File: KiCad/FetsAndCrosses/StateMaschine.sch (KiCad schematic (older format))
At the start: 0 parts

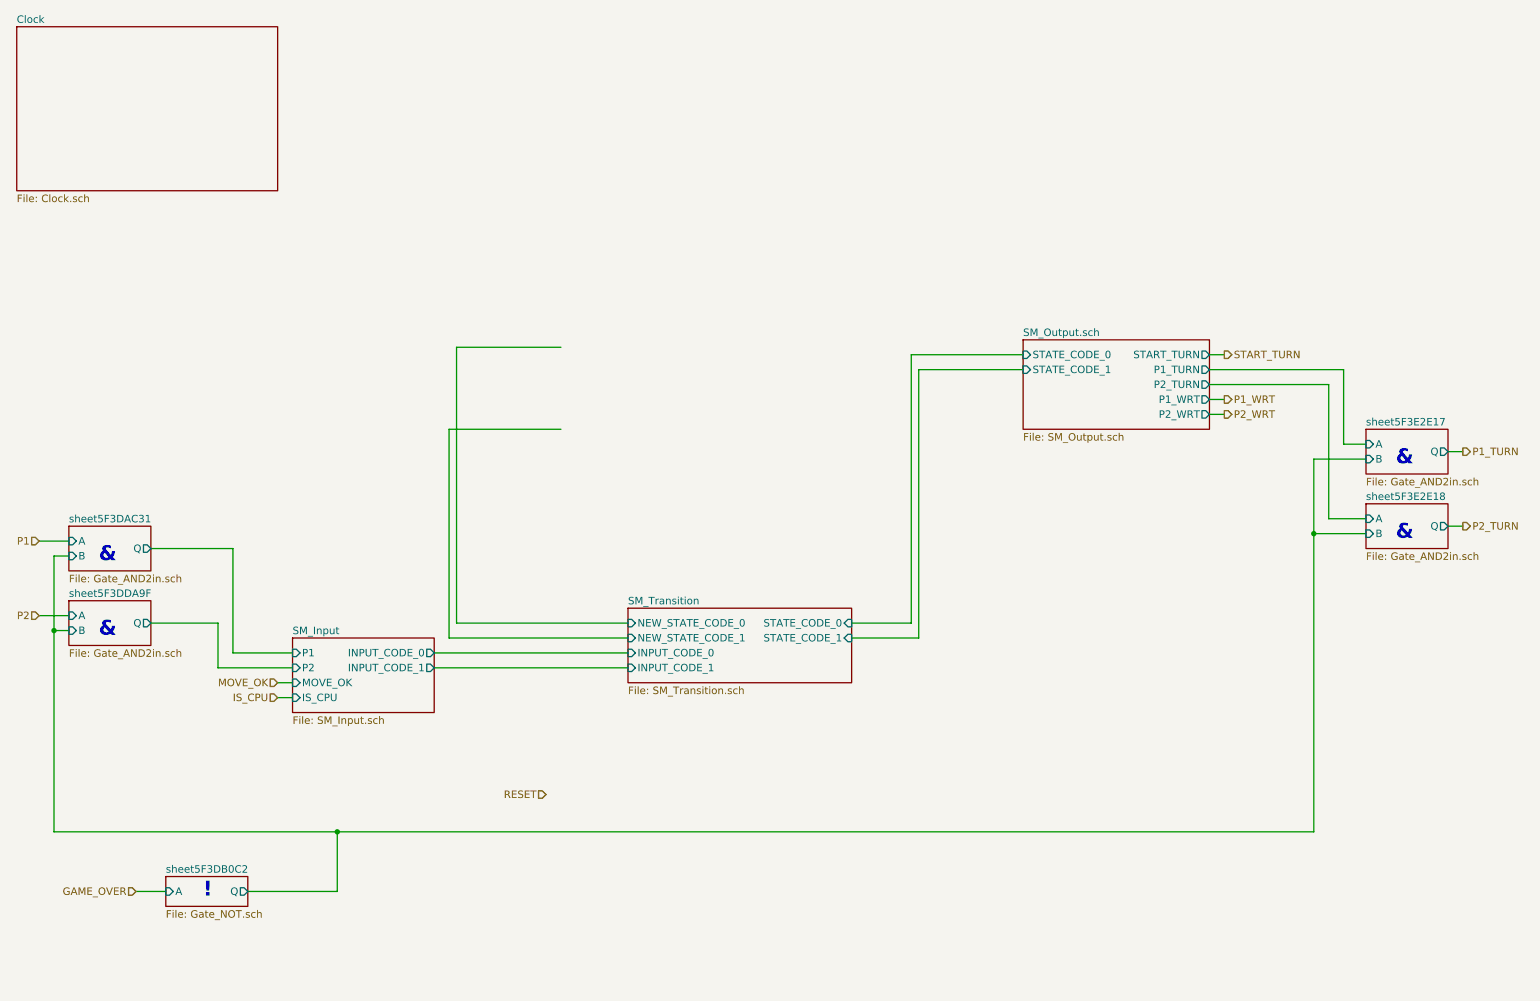
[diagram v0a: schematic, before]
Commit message: Reworked everything to use Buses
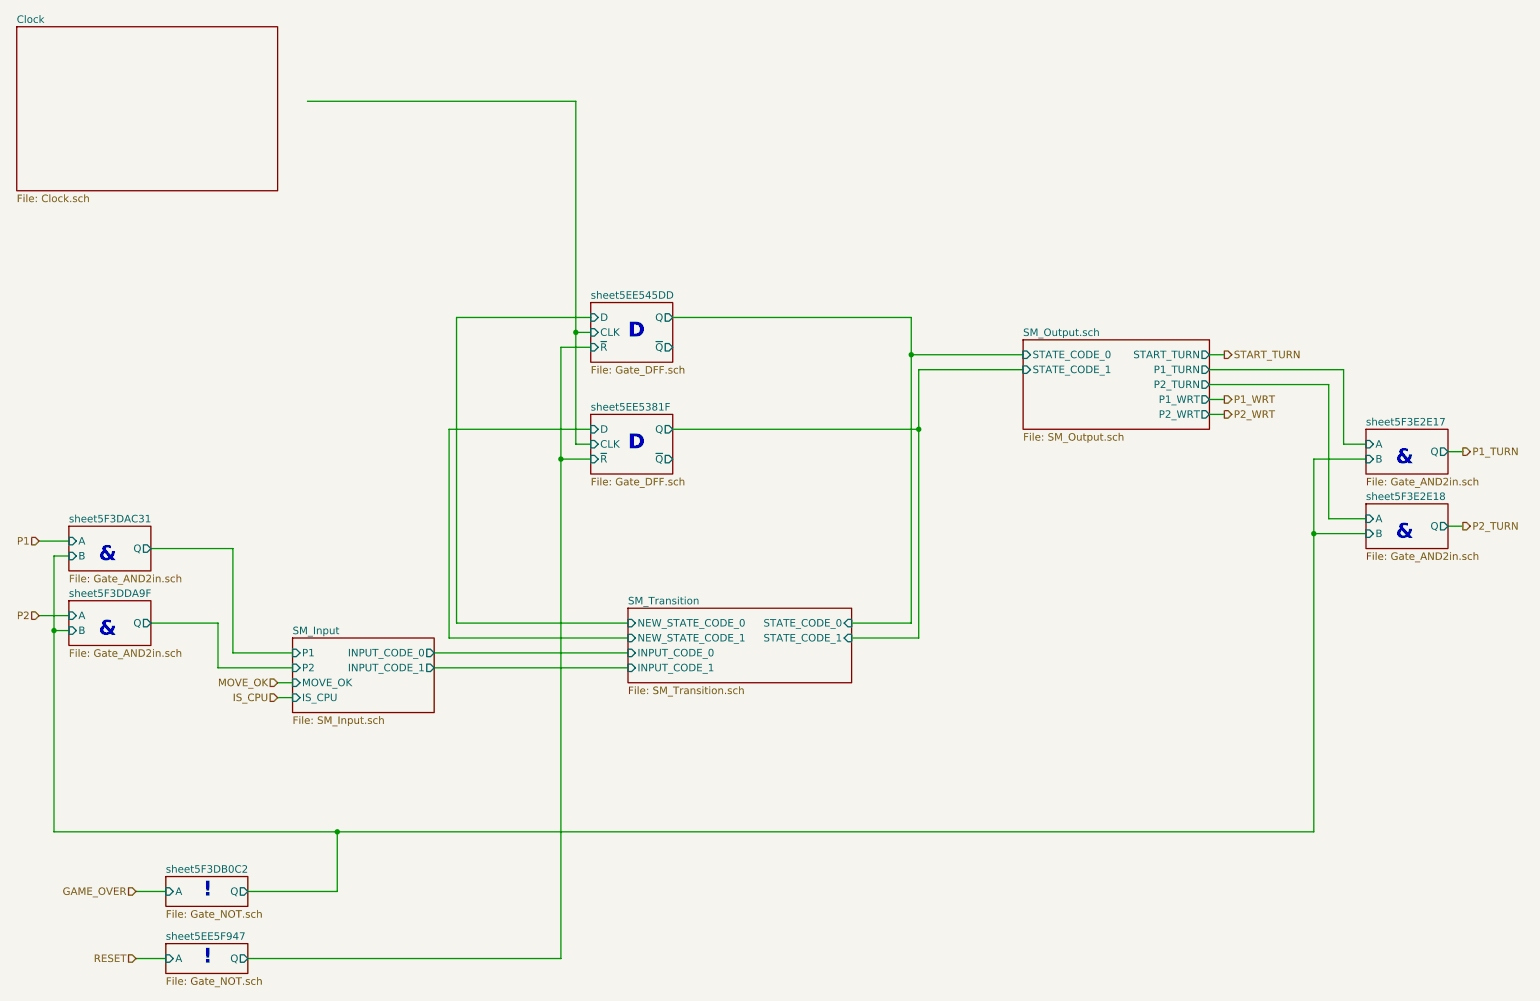
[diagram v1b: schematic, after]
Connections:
- wire segments 48 -> 63
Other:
- note added: "D"
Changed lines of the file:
@@
 $Descr A4 11693 8268
 encoding utf-8
-Sheet 167 215
+Sheet 170 400
 Title ""
 Date ""
@@
 	7700 3000 7000 3000
 Wire Wire Line
-	7000 3000 7000 4800
+	7000 3000 7000 3400
 Wire Wire Line
 	7000 4800 6550 4800
@@
 	3850 4800 3850 3400
 Wire Wire Line
-	3850 3400 4600 3400
-Wire Wire Line
 	5050 4700 3900 4700
 Wire Wire Line
-	3900 4700 3900 2850
-Wire Wire Line
-	3900 2850 4600 2850
-Text HLabel 4500 5850 0    50   Input ~ 0
+	3900 4700 3900 2650
+Text HLabel 1750 6950 0    50   Input ~ 0
 RESET
 Text HLabel 9050 2900 2    50   Output ~ 0
@@
 Connection ~ 9650 4100
 Connection ~ 3100 6100
+$Sheet
+S 4800 3300 550  400
+U 5EE53826
+F0 "sheet5EE5381F" 50
+F1 "Gate_DFF.sch" 50
+F2 "D" I L 4800 3400 50
+F3 "CLK" I L 4800 3500 50
+F4 "Q" O R 5350 3400 50
+F5 "~Q" O R 5350 3600 50
+F6 "~R" I L 4800 3600 50
+$EndSheet
+Text Notes 5050 3550 0    100  ~ 20
+D
+$Sheet
+S 4800 2550 550  400
+U 5EE545E4
+F0 "sheet5EE545DD" 50
+F1 "Gate_DFF.sch" 50
+F2 "D" I L 4800 2650 50
+F3 "CLK" I L 4800 2750 50
+F4 "Q" O R 5350 2650 50
+F5 "~Q" O R 5350 2850 50
+F6 "~R" I L 4800 2850 50
+$EndSheet
+Text Notes 5050 2800 0    100  ~ 20
+D
+Wire Wire Line
+	3900 2650 4800 2650
+Wire Wire Line
+	3850 3400 4800 3400
+Wire Wire Line
+	4800 3500 4700 3500
+Wire Wire Line
+	4700 3500 4700 2750
+Wire Wire Line
+	4700 2750 4800 2750
+Wire Wire Line
+	4700 2750 4700 1200
+Wire Wire Line
+	4700 1200 2900 1200
+Connection ~ 4700 2750
+Wire Wire Line
+	4800 3600 4600 3600
+Wire Wire Line
+	4600 3600 4600 2850
+Wire Wire Line
+	4600 2850 4800 2850
+Wire Wire Line
+	4600 3600 4600 6950
+Connection ~ 4600 3600
+$Sheet
+S 1950 6850 550  200
+U 5EE5F94B
+F0 "sheet5EE5F947" 50
+F1 "Gate_NOT.sch" 50
+F2 "A" I L 1950 6950 50
+F3 "Q" O R 2500 6950 50
+$EndSheet
+Text Notes 2200 7000 0    100  ~ 20
+!
+Wire Wire Line
+	2500 6950 4600 6950
+Wire Wire Line
+	1750 6950 1950 6950
+Wire Wire Line
+	6950 2900 6950 2650
+Wire Wire Line
+	6950 2650 5350 2650
+Connection ~ 6950 2900
+Wire Wire Line
+	5350 3400 7000 3400
+Connection ~ 7000 3400
+Wire Wire Line
+	7000 3400 7000 4800
 $EndSCHEMATC

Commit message: Schematic Done, Footprints assigned, ERC OK.
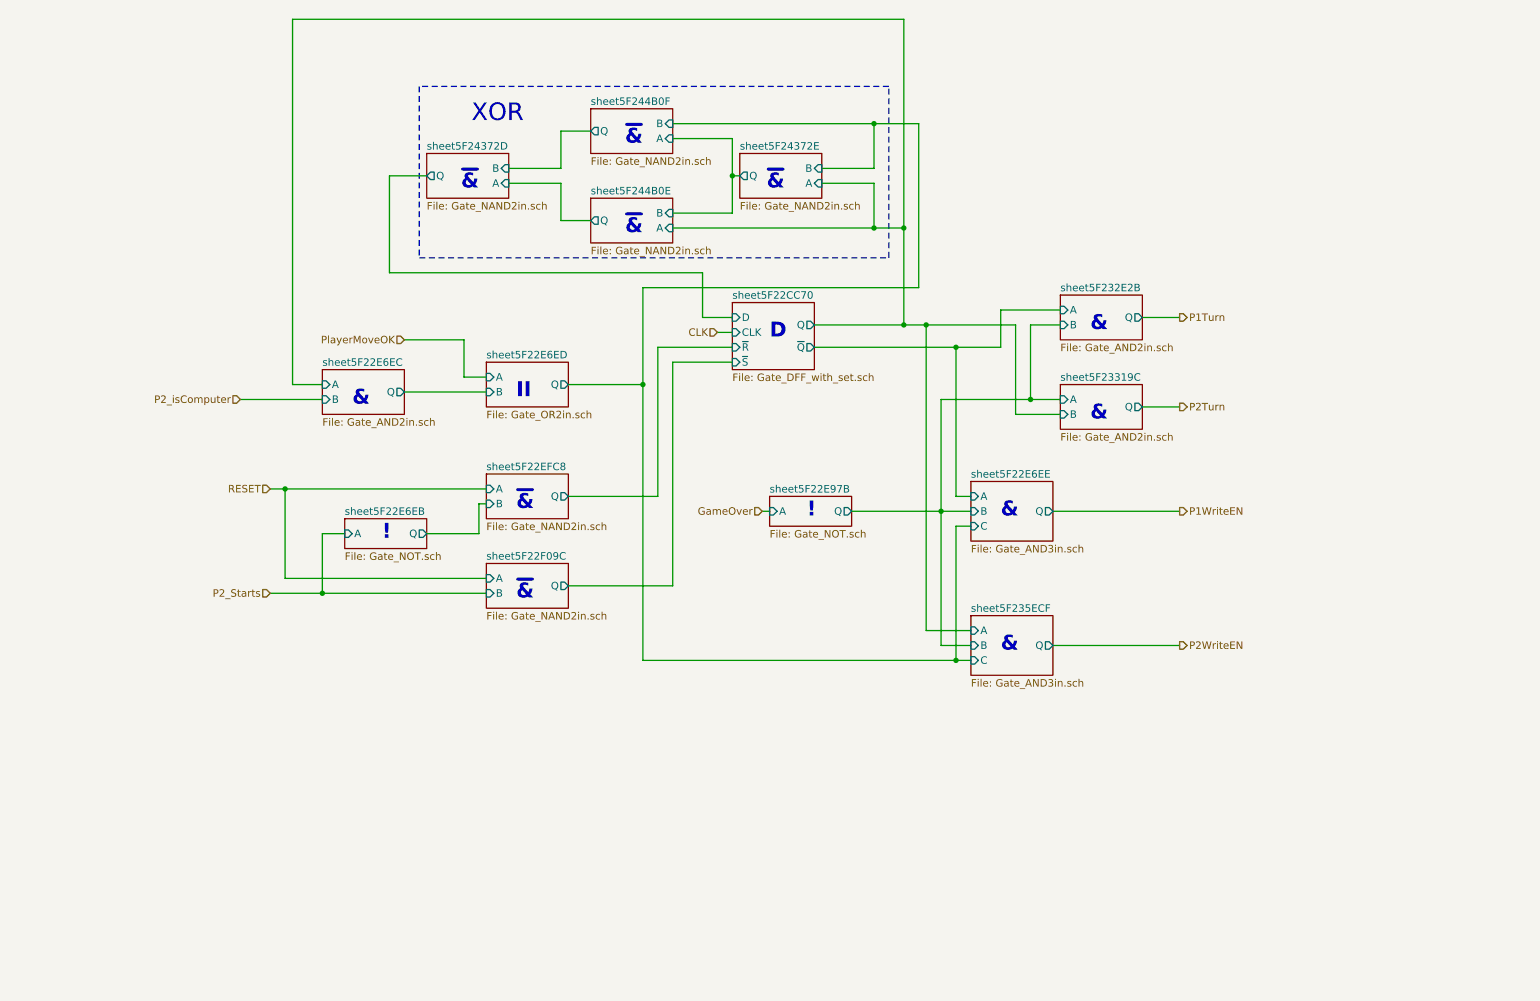
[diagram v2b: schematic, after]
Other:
- note added: "II"
- note added: "XOR"
- note added: "~&"

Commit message: First Draft Schematic Updates
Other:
- note added: "Accept Move Logic\n"
- note added: "Output Decoding"
- note added: "Select Right Player on Reset"
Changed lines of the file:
@@
 $Descr A4 11693 8268
 encoding utf-8
-Sheet 159 389
+Sheet 149 360
 Title ""
 Date "2020-07-05"
@@
 $EndSheet
 $Sheet
-S 3150 4000 550  200
+S 3100 5400 550  200
 U 5F22E6F2
 F0 "sheet5F22E6EB" 50
 F1 "Gate_NOT.sch" 50
-F2 "A" I L 3150 4100 50
-F3 "Q" O R 3700 4100 50
+F2 "A" I L 3100 5500 50
+F3 "Q" O R 3650 5500 50
 $EndSheet
 $Sheet
@@
 $EndSheet
 $Sheet
-S 7350 3750 550  400
+S 8550 3750 550  400
 U 5F22E705
 F0 "sheet5F22E6EE" 50
 F1 "Gate_AND3in.sch" 50
-F2 "A" I L 7350 3850 50
-F3 "B" I L 7350 3950 50
-F4 "C" I L 7350 4050 50
-F5 "Q" O R 7900 3950 50
-$EndSheet
-$Sheet
-S 6000 3850 550  200
+F2 "A" I L 8550 3850 50
+F3 "B" I L 8550 3950 50
+F4 "C" I L 8550 4050 50
+F5 "Q" O R 9100 3950 50
+$EndSheet
+$Sheet
+S 7200 3850 550  200
 U 5F22E97F
 F0 "sheet5F22E97B" 50
 F1 "Gate_NOT.sch" 50
-F2 "A" I L 6000 3950 50
-F3 "Q" O R 6550 3950 50
-$EndSheet
-$Sheet
-S 4100 3700 550  300
+F2 "A" I L 7200 3950 50
+F3 "Q" O R 7750 3950 50
+$EndSheet
+$Sheet
+S 4050 5100 550  300
 U 5F22EFCE
 F0 "sheet5F22EFC8" 50
 F1 "Gate_NAND2in.sch" 50
-F2 "Q" O R 4650 3850 50
-F3 "A" I L 4100 3800 50
-F4 "B" I L 4100 3900 50
-$EndSheet
-$Sheet
-S 4100 4300 550  300
+F2 "Q" O R 4600 5250 50
+F3 "A" I L 4050 5200 50
+F4 "B" I L 4050 5300 50
+$EndSheet
+$Sheet
+S 4050 5700 550  300
 U 5F22F0A2
 F0 "sheet5F22F09C" 50
 F1 "Gate_NAND2in.sch" 50
-F2 "Q" O R 4650 4450 50
-F3 "A" I L 4100 4400 50
-F4 "B" I L 4100 4500 50
-$EndSheet
-$Sheet
-S 7950 2500 550  300
+F2 "Q" O R 4600 5850 50
+F3 "A" I L 4050 5800 50
+F4 "B" I L 4050 5900 50
+$EndSheet
+$Sheet
+S 9150 2500 550  300
 U 5F232E31
 F0 "sheet5F232E2B" 50
 F1 "Gate_AND2in.sch" 50
-F2 "A" I L 7950 2600 50
-F3 "B" I L 7950 2700 50
-F4 "Q" O R 8500 2650 50
-$EndSheet
-$Sheet
-S 7950 3100 550  300
+F2 "A" I L 9150 2600 50
+F3 "B" I L 9150 2700 50
+F4 "Q" O R 9700 2650 50
+$EndSheet
+$Sheet
+S 9150 3100 550  300
 U 5F2331A2
 F0 "sheet5F23319C" 50
 F1 "Gate_AND2in.sch" 50
-F2 "A" I L 7950 3200 50
-F3 "B" I L 7950 3300 50
-F4 "Q" O R 8500 3250 50
-$EndSheet
-$Sheet
-S 7350 4650 550  400
+F2 "A" I L 9150 3200 50
+F3 "B" I L 9150 3300 50
+F4 "Q" O R 9700 3250 50
+$EndSheet
+$Sheet
+S 8550 4650 550  400
 U 5F235ED5
 F0 "sheet5F235ECF" 50
 F1 "Gate_AND3in.sch" 50
-F2 "A" I L 7350 4750 50
-F3 "B" I L 7350 4850 50
-F4 "C" I L 7350 4950 50
-F5 "Q" O R 7900 4850 50
+F2 "A" I L 8550 4750 50
+F3 "B" I L 8550 4850 50
+F4 "C" I L 8550 4950 50
+F5 "Q" O R 9100 4850 50
 $EndSheet
 $Sheet
@@
 Text HLabel 2450 3200 0    50   Input ~ 0
 P2_isComputer
-Text HLabel 2650 4500 0    50   Input ~ 0
+Text HLabel 2600 5900 0    50   Input ~ 0
 P2_Starts
-Text HLabel 5950 3950 0    50   Input ~ 0
+Text HLabel 7150 3950 0    50   Input ~ 0
 GameOver
 Text HLabel 5650 2750 0    50   Input ~ 0
 CLK
-Text HLabel 2650 3800 0    50   Input ~ 0
+Text HLabel 2600 5200 0    50   Input ~ 0
 RESET
-Text HLabel 8750 2650 2    50   Output ~ 0
+Text HLabel 9950 2650 2    50   Output ~ 0
 P1Turn
-Text HLabel 8750 3250 2    50   Output ~ 0
+Text HLabel 9950 3250 2    50   Output ~ 0
 P2Turn
-Text HLabel 8750 3950 2    50   Output ~ 0
+Text HLabel 9950 3950 2    50   Output ~ 0
 P1WriteEN
-Text HLabel 8750 4850 2    50   Output ~ 0
+Text HLabel 9950 4850 2    50   Output ~ 0
 P2WriteEN
 Text Notes 6000 2800 0    100  ~ 20
 D
-Text Notes 3400 4150 0    100  ~ 20
+Text Notes 3350 5550 0    100  ~ 20
 !
 Text Notes 3200 3250 0    100  ~ 20
@@
 Text Notes 4300 3200 0    100  ~ 20
 II
-Text Notes 7550 4000 0    100  ~ 20
+Text Notes 8750 4000 0    100  ~ 20
 &
-Text Notes 6250 4000 0    100  ~ 20
+Text Notes 7450 4000 0    100  ~ 20
 !
-Text Notes 4300 3950 0    100  ~ 20
-~&
-Text Notes 4300 4550 0    100  ~ 20
-~&
-Text Notes 8150 2750 0    100  ~ 20
+Text Notes 4250 5350 0    100  ~ 20
+~&
+Text Notes 4250 5950 0    100  ~ 20
+~&
+Text Notes 9350 2750 0    100  ~ 20
 &
-Text Notes 8150 3350 0    100  ~ 20
+Text Notes 9350 3350 0    100  ~ 20
 &
-Text Notes 7550 4900 0    100  ~ 20
+Text Notes 8750 4900 0    100  ~ 20
 &
 Text Notes 4050 1800 2    100  ~ 20
@@
 XOR
 Wire Wire Line
-	4650 3850 5250 3850
-Wire Wire Line
-	5250 3850 5250 2850
-Wire Wire Line
 	5250 2850 5750 2850
 Wire Wire Line
 	5750 2950 5350 2950
 Wire Wire Line
-	5350 2950 5350 4450
-Wire Wire Line
-	5350 4450 4650 4450
-Wire Wire Line
-	2650 3800 2750 3800
-Wire Wire Line
-	4100 4400 2750 4400
-Wire Wire Line
-	2750 4400 2750 3800
-Wire Wire Line
-	2750 3800 4100 3800
-Wire Wire Line
-	3700 4100 4050 4100
-Wire Wire Line
-	4050 4100 4050 3900
-Wire Wire Line
-	4050 3900 4100 3900
-Wire Wire Line
-	3150 4100 3000 4100
-Wire Wire Line
-	3000 4100 3000 4500
-Wire Wire Line
-	3000 4500 4100 4500
-Wire Wire Line
-	3000 4500 2650 4500
+	2600 5200 2700 5200
+Wire Wire Line
+	4050 5800 2700 5800
+Wire Wire Line
+	2700 5800 2700 5200
+Wire Wire Line
+	2700 5200 4050 5200
+Wire Wire Line
+	3650 5500 4000 5500
+Wire Wire Line
+	4000 5500 4000 5300
+Wire Wire Line
+	4000 5300 4050 5300
+Wire Wire Line
+	3100 5500 2950 5500
+Wire Wire Line
+	2950 5500 2950 5900
+Wire Wire Line
+	2950 5900 4050 5900
+Wire Wire Line
+	2950 5900 2600 5900
 Wire Wire Line
 	4100 3150 3550 3150
@@
 	3950 3050 4100 3050
 Wire Wire Line
-	8500 3250 8750 3250
-Wire Wire Line
-	8500 2650 8750 2650
-Wire Wire Line
-	7950 2700 7750 2700
-Wire Wire Line
-	7750 2700 7750 3200
-Wire Wire Line
-	7750 3200 7950 3200
-Wire Wire Line
-	7950 3300 7650 3300
-Wire Wire Line
-	7650 3300 7650 2700
-Wire Wire Line
-	7650 2700 7050 2700
-Wire Wire Line
-	6300 2850 7250 2850
-Wire Wire Line
-	7550 2850 7550 2600
-Wire Wire Line
-	7550 2600 7950 2600
-Wire Wire Line
-	7900 4850 8750 4850
-Wire Wire Line
-	8750 3950 7900 3950
-Wire Wire Line
-	7350 3850 7250 3850
-Wire Wire Line
-	7250 3850 7250 2850
-Wire Wire Line
-	7250 2850 7550 2850
-Wire Wire Line
-	7050 2700 7050 4750
-Wire Wire Line
-	7050 4750 7350 4750
-Wire Wire Line
-	7050 2700 6900 2700
-Wire Wire Line
-	7150 3950 7150 3200
-Wire Wire Line
-	7150 3200 7750 3200
-Wire Wire Line
-	7150 3950 7350 3950
-Wire Wire Line
-	6550 3950 7150 3950
-Wire Wire Line
-	5950 3950 6000 3950
-Wire Wire Line
-	7150 3950 7150 4850
-Wire Wire Line
-	7150 4850 7350 4850
-Wire Wire Line
-	7350 4050 7250 4050
-Wire Wire Line
-	7250 4050 7250 4950
-Wire Wire Line
-	7250 4950 7350 4950
-Wire Wire Line
-	7250 4950 5150 4950
+	9700 3250 9950 3250
+Wire Wire Line
+	9700 2650 9950 2650
+Wire Wire Line
+	9150 2700 8950 2700
+Wire Wire Line
+	8950 2700 8950 3200
+Wire Wire Line
+	8950 3200 9150 3200
+Wire Wire Line
+	9150 3300 8850 3300
+Wire Wire Line
+	8850 3300 8850 2700
+Wire Wire Line
+	8850 2700 8250 2700
+Wire Wire Line
+	8750 2850 8750 2600
+Wire Wire Line
+	8750 2600 9150 2600
+Wire Wire Line
+	9100 4850 9950 4850
+Wire Wire Line
+	9950 3950 9100 3950
+Wire Wire Line
+	8550 3850 8450 3850
+Wire Wire Line
+	8450 3850 8450 2850
+Wire Wire Line
+	8450 2850 8750 2850
+Wire Wire Line
+	8250 2700 8250 4750
+Wire Wire Line
+	8250 4750 8550 4750
+Wire Wire Line
+	8350 3950 8350 3200
+Wire Wire Line
+	8350 3200 8950 3200
+Wire Wire Line
+	8350 3950 8550 3950
+Wire Wire Line
+	7750 3950 8350 3950
+Wire Wire Line
+	7150 3950 7200 3950
+Wire Wire Line
+	8350 3950 8350 4850
+Wire Wire Line
+	8350 4850 8550 4850
+Wire Wire Line
+	8550 4050 8450 4050
+Wire Wire Line
+	8450 4050 8450 4950
+Wire Wire Line
+	8450 4950 8550 4950
 Wire Wire Line
 	5150 4950 5150 3100
@@
 Wire Wire Line
 	6900 2700 6900 2050
-Wire Wire Line
-	6900 2700 6300 2700
 Wire Wire Line
 	4250 1650 4600 1650
@@
 Wire Wire Line
 	6900 650  6900 2050
-Connection ~ 2750 3800
-Connection ~ 3000 4500
-Connection ~ 7250 2850
-Connection ~ 7050 2700
-Connection ~ 7750 3200
-Connection ~ 7150 3950
-Connection ~ 7250 4950
-Connection ~ 6900 2700
+Connection ~ 2700 5200
+Connection ~ 2950 5900
+Connection ~ 8450 2850
+Connection ~ 8250 2700
+Connection ~ 8950 3200
+Connection ~ 8350 3950
+Connection ~ 8450 4950
 Connection ~ 5750 1700
 Connection ~ 6700 1350
@@
 Connection ~ 5150 3100
 Connection ~ 6900 2050
+Wire Wire Line
+	4600 5250 5250 5250
+Wire Wire Line
+	5250 2850 5250 5250
+Wire Wire Line
+	5350 2950 5350 5850
+Wire Wire Line
+	4600 5850 5350 5850
+Text Notes 2900 5000 0    50   ~ 0
+Select Right Player on Reset
+Wire Wire Line
+	6300 2850 8450 2850
+Wire Wire Line
+	6300 2700 6900 2700
+Connection ~ 6900 2700
+Wire Wire Line
+	6900 2700 8250 2700
+Wire Wire Line
+	5150 4950 8450 4950
+Text Notes 8300 2450 0    50   ~ 0
+Output Decoding
+Text Notes 1850 1000 0    50   ~ 0
+Accept Move Logic\n
 $EndSCHEMATC
